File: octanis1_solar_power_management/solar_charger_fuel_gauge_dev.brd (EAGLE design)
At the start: 100 x 58.4 mm, 92 parts, among them IC401 TUSB2046BIRHBIRHB, Q2 32.768kHz, Q4 CSTCR4M00G15L99, Q401 CSTCR6M00G15L99, U1 BQ24210, U2 BQ27510_DRZ_12, U402 TPS62237DRY, U404 TPD2E001DRLR, U6 MSP430F5529IPNR

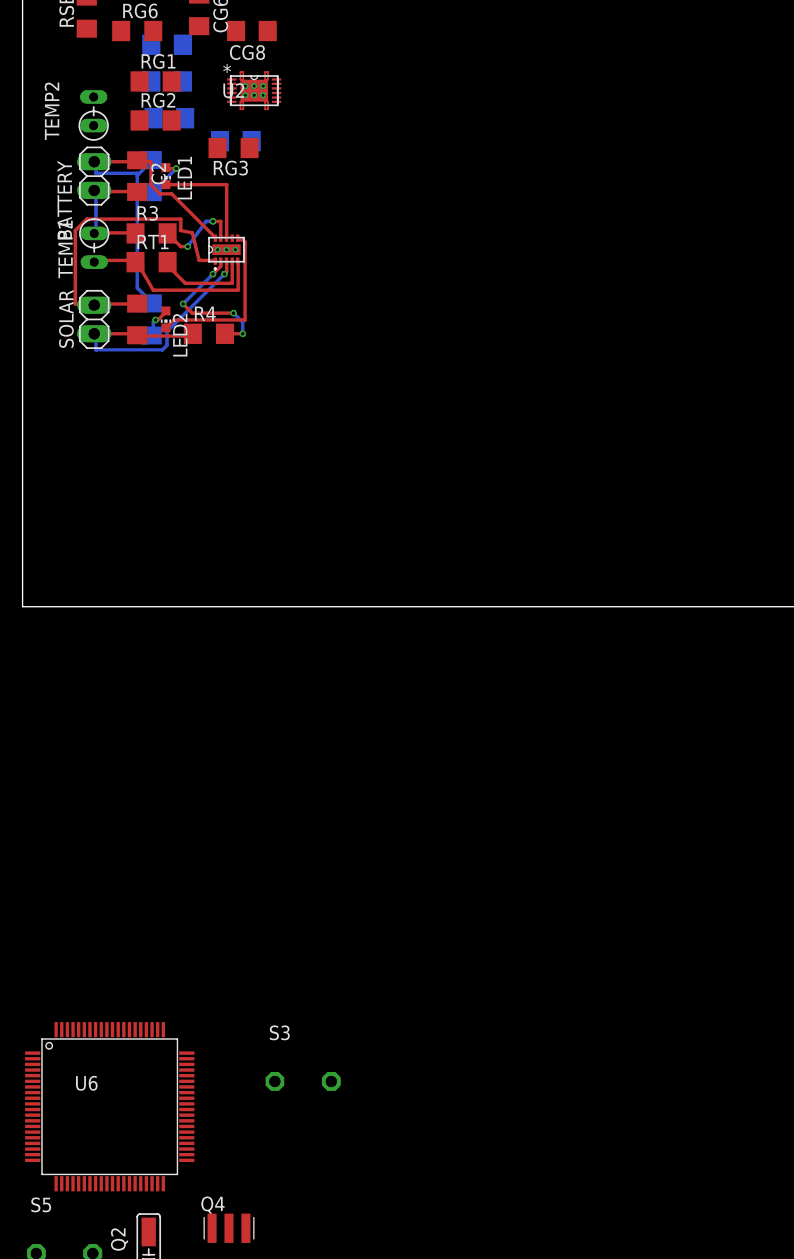
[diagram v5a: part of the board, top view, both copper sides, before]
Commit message: Rearranged some components and routes and increased thickness of power lines
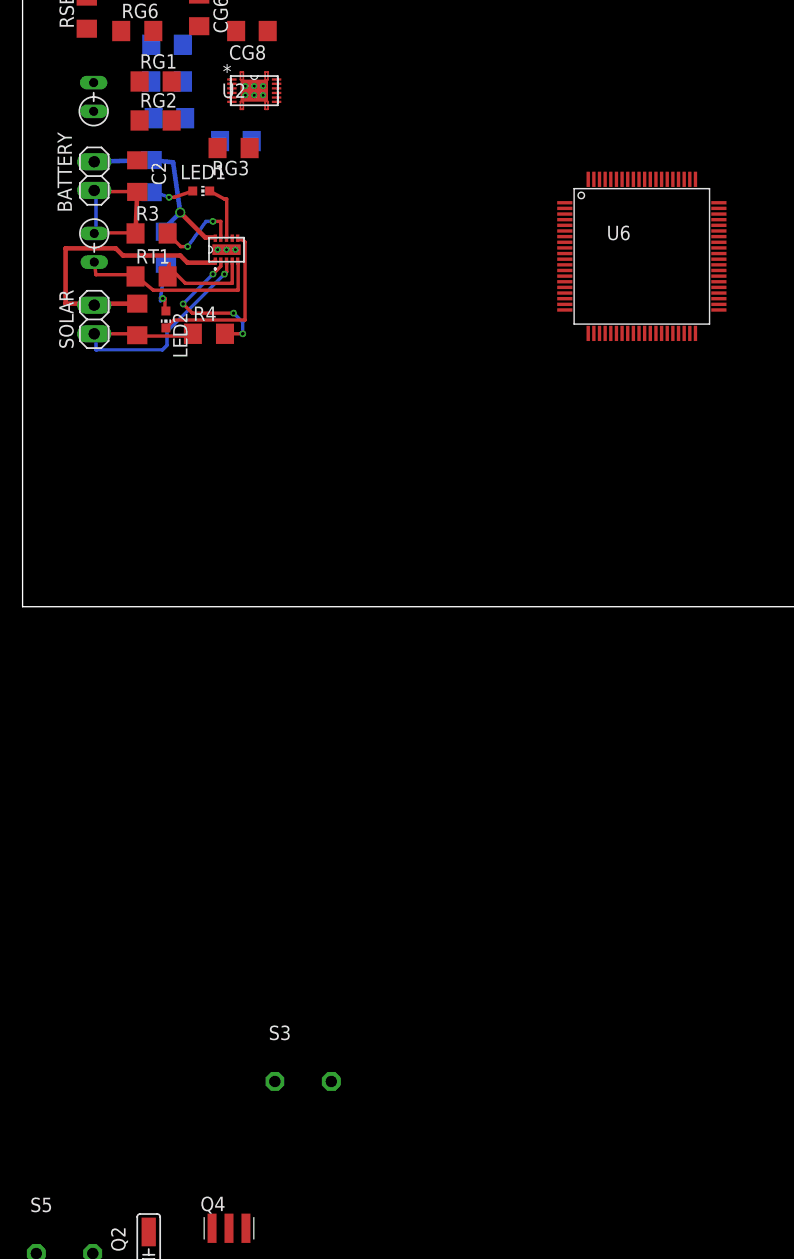
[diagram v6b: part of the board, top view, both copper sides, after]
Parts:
- R1, R2: value (none) -> 1k
- moved U6 88.9 mm to (54.9, 31.0)
- moved R2 6.48 mm to (12.7, 31.8)
- moved LED1 3.39 mm to (15.8, 36.8), turned to 270 degrees
- moved TEMP2 1.27 mm to (6.30, 45.2)
- moved RT1 1.27 mm to (11.4, 29.3)
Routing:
- net BAT+: track 33.6 -> 18.6 mm, vias 0 -> 1
- net N$4: track 10.1 -> 5.16 mm
- net GND: track 7.21 -> 11.7 mm
- net N$3: track 2.80 -> 5.32 mm
- net N$13: track 27.9 -> 29.0 mm
- net N$8: track 8.65 -> 9.56 mm

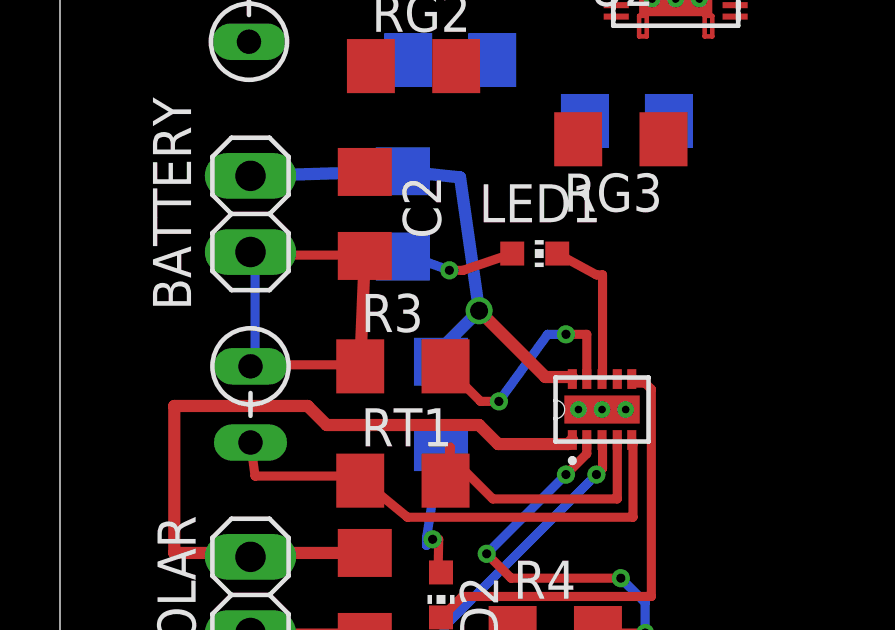
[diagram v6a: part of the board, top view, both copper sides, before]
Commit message: Calculated R-values for Battery chargin circuit
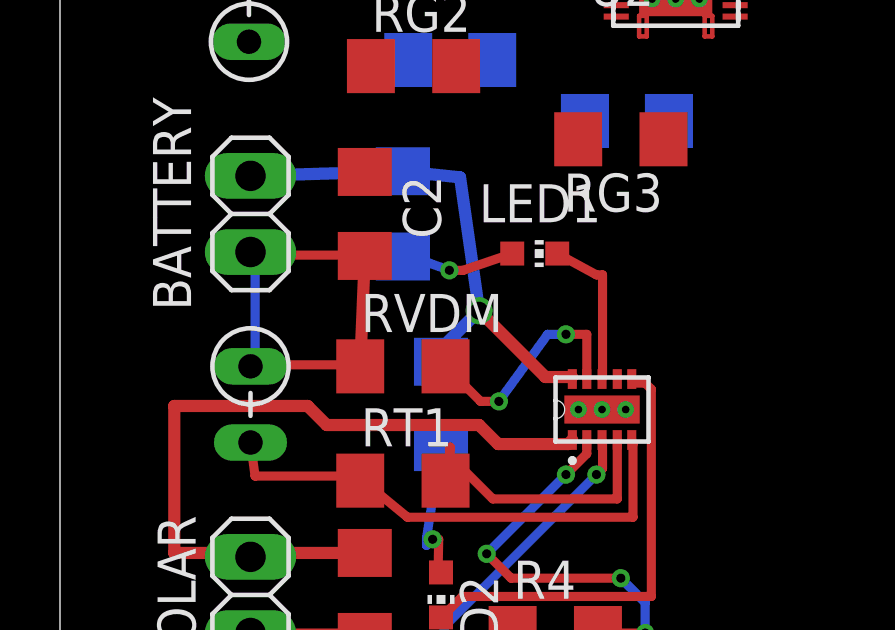
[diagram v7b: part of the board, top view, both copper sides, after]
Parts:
- R4: value (none) -> 500
- RT1: value (none) -> 21.5k
- RVDM: value (none) -> float
- renumbered R3 to RVDM
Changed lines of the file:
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@@
 <attribute name="VALUE" x="6.985" y="34.3408" size="1.27" layer="27" ratio="10" rot="R270"/>
 </element>
-<element name="RT1" library="resistor" package="R1206" value="" x="11.43" y="29.2608"/>
+<element name="RT1" library="resistor" package="R1206" value="21.5k" x="11.43" y="29.2608"/>
 <element name="BATTERY" library="pinhead" package="1X02" value="" x="6.35" y="38.1508" smashed="yes" rot="R270">
 <attribute name="NAME" x="3.0988" y="42.037" size="1.27" layer="25" ratio="10" rot="R270"/>
 <attribute name="VALUE" x="3.175" y="40.6908" size="1.27" layer="27" rot="R270"/>
 </element>
-<element name="R3" library="resistor" package="R1206" value="" x="11.43" y="33.0708"/>
-<element name="R4" library="resistor" package="R1206" value="" x="16.51" y="24.1808"/>
+<element name="RVDM" library="resistor" package="R1206" value="float" x="11.43" y="33.0708"/>
+<element name="R4" library="resistor" package="R1206" value="500" x="16.51" y="24.1808"/>
 <element name="SOLAR" library="pinhead" package="1X02" value="" x="6.35" y="25.4508" smashed="yes" rot="R90">
 <attribute name="NAME" x="4.5212" y="22.8346" size="1.27" layer="25" ratio="10" rot="R90"/>
@@
 <signal name="GND">
 <contactref element="C2" pad="2"/>
-<contactref element="R3" pad="1"/>
+<contactref element="RVDM" pad="1"/>
 <wire x1="6.5024" y1="33.1216" x2="9.9568" y2="33.1216" width="0.3048" layer="1"/>
 <wire x1="9.9568" y1="33.1216" x2="10.008" y2="33.0708" width="0.3048" layer="1"/>
@@
 <signal name="N$6">
 <contactref element="U1" pad="9"/>
-<contactref element="R3" pad="2"/>
+<contactref element="RVDM" pad="2"/>
 <wire x1="16.256" y1="34.1376" x2="14.6304" y2="31.9024" width="0.3048" layer="16"/>
 <via x="14.6304" y="31.9024" extent="1-16" drill="0.3048" diameter="0.254"/>

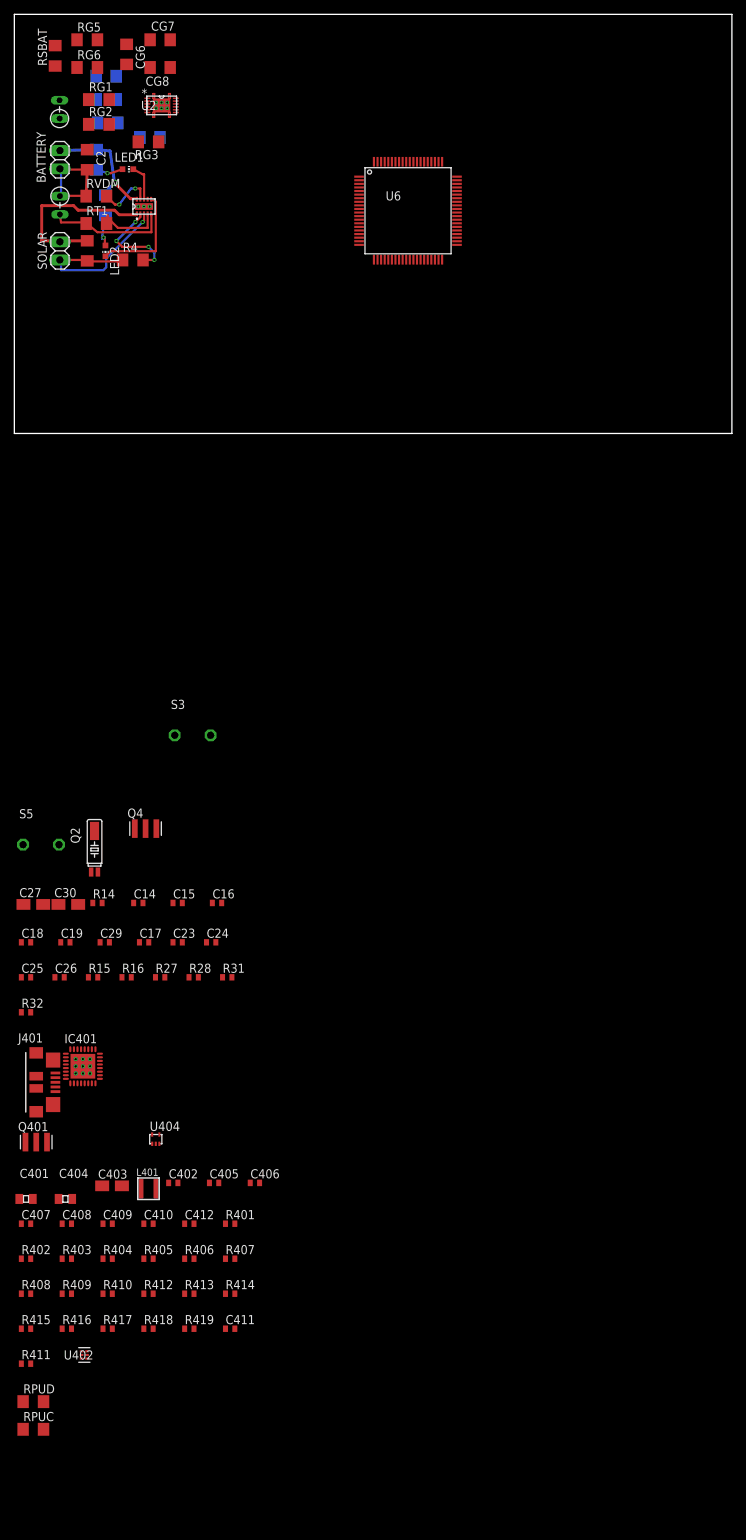
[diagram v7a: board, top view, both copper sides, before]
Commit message: changed PCB-size and Added 5V-booster circuit
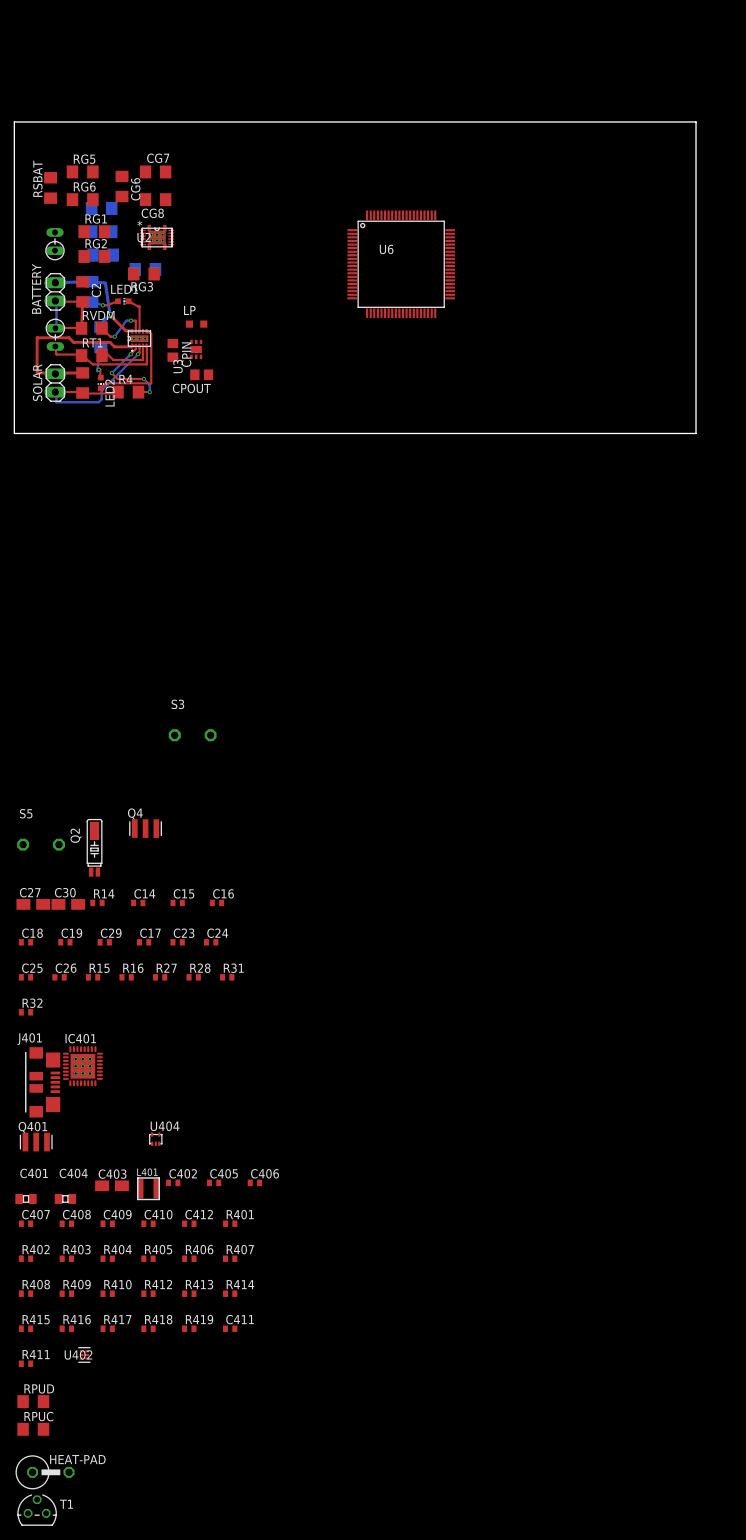
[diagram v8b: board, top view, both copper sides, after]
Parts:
- added CPIN: 2.2uF, rcl:C0805
- added CPOUT: 4.7uF, rcl:C0805
- added HEAT-PAD: (no value), resistor:P0613V
- added LP: 1uH, eagle-ltspice:L2012C
- added T1: BC547, transistor:TO92
- added U3: TPS61240DRVT, TPS61240DRVT:SON65P200X200X80-7N
- moved CG1 18.4 mm to (18.3, 22.8)
- moved CG3 18.4 mm to (12.2, 28.1)
- moved R4 18.4 mm to (15.9, 5.77)
- moved RG1 18.4 mm to (11.2, 28.1)
- moved RG2 18.4 mm to (11.2, 24.7)
- moved C1 18.4 mm to (9.53, 7.04)
- moved CG2 18.4 mm to (12.2, 31.4)
- moved CG4 18.4 mm to (12.4, 24.9)
- moved CG6 18.4 mm to (15.0, 34.4)
- moved CG7 18.4 mm to (19.7, 36.4)
- moved CG8 18.4 mm to (19.7, 32.6)
- moved LED1 18.4 mm to (15.2, 18.4)
- moved LED2 18.4 mm to (12.1, 7.04)
- moved R2 18.4 mm to (12.1, 13.4)
- moved RG3 18.4 mm to (18.1, 22.2)
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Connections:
- new net 5V: CPOUT.1, U3.2, U3.3
- new net EN5V: U3.4
- new net N$37: HEAT-PAD.1, T1.3
- new net N$39: T1.1
- new net N$40: T1.2
- new net N$41: LP.2, U3.5
- net +3V3: now also HEAT-PAD.2
- net BAT+: now also CPIN.1, LP.1, U3.6
- net GND: now also CPIN.2, CPOUT.2, U3.1
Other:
- board size 100 x 58.4 mm -> 95 x 43.4 mm
